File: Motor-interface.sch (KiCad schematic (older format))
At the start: 25 parts, among them K1 RELAY_2RT, P2 TE-23pins connector, Q1 Q_NPN_BCE, U1 MCP42010, U2 Teensy_3.2

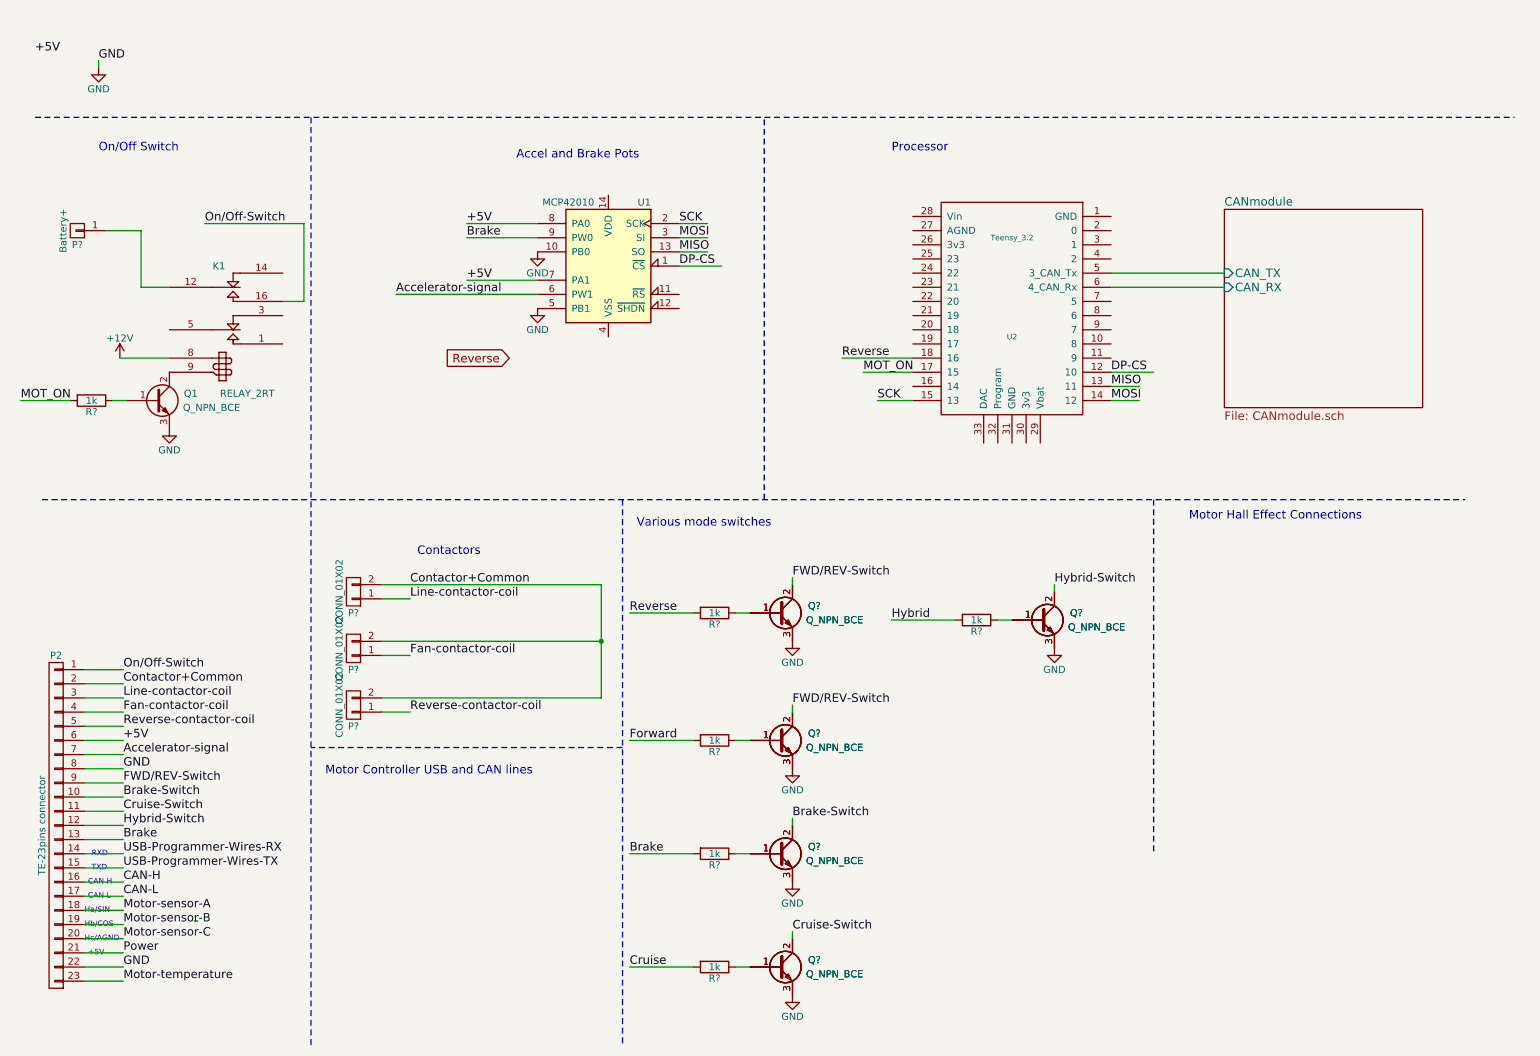
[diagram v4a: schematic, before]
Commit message: added hall effect connector and USB and CAN lines
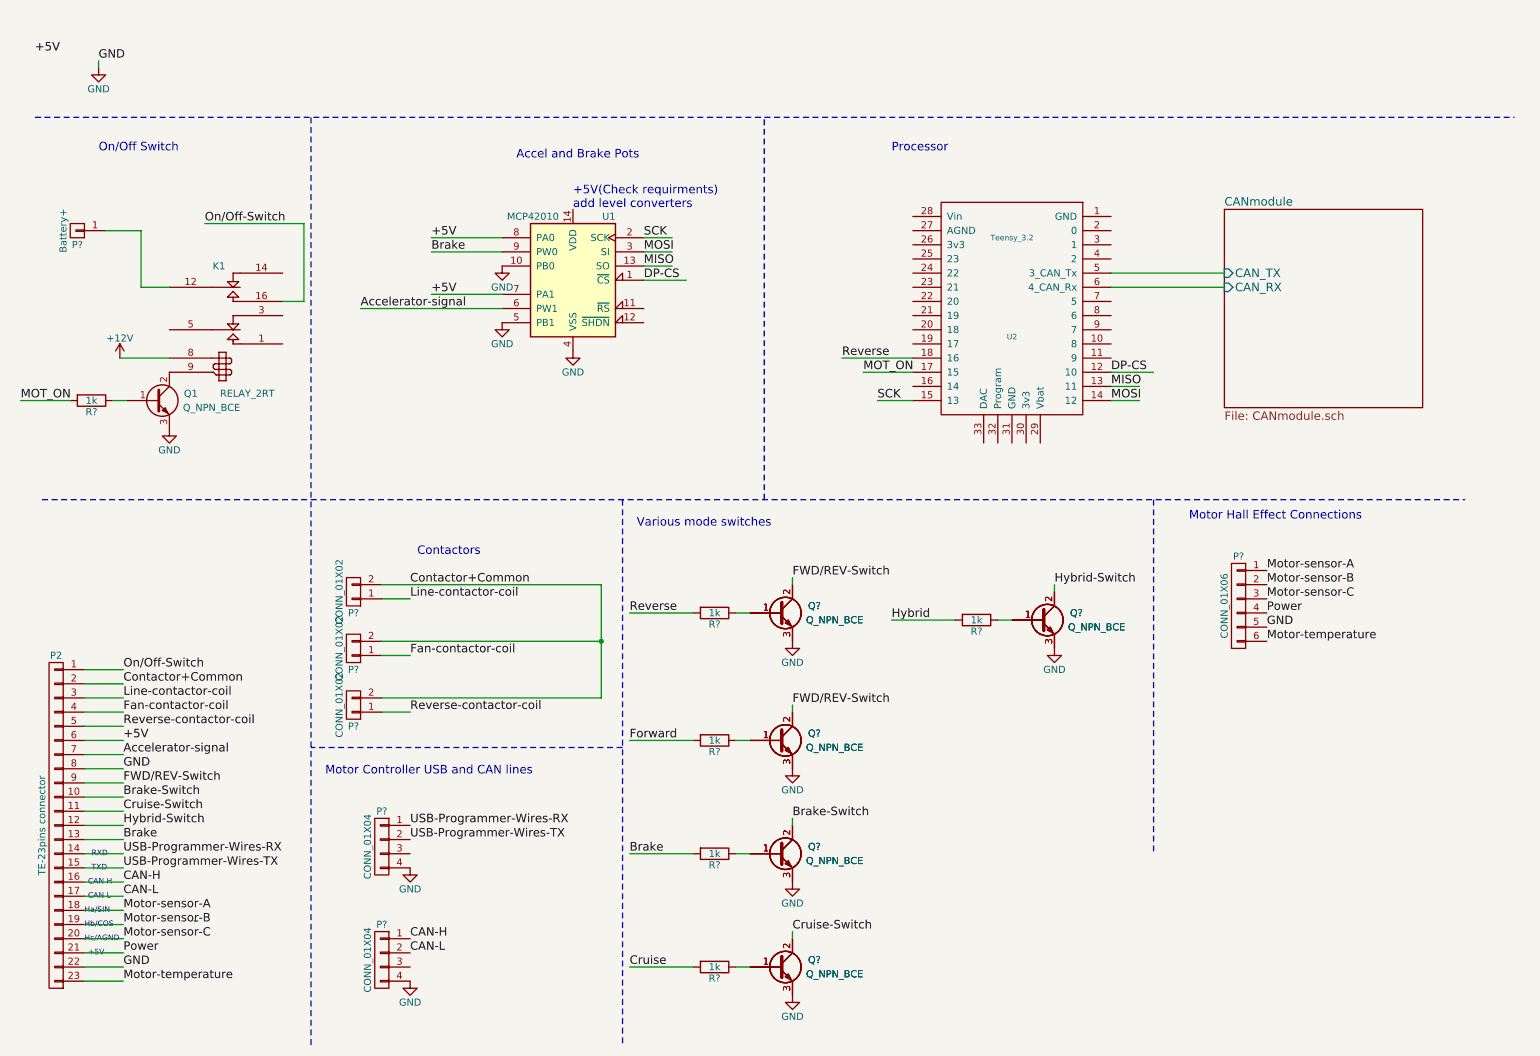
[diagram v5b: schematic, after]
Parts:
- added P?: CONN_01X06, symbol CONN_01X06
- added P? (x2): CONN_01X04, symbol CONN_01X04
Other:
- note added: "+5V(Check requirments)\nadd level converters"
- moved on the sheet: U1
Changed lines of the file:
@@
 LIBS:contrib
 LIBS:valves
-LIBS:electric_car
 LIBS:Motor-interface-cache
 EELAYER 25 0
@@
 L MCP42010 U1
 U 1 1 57FC991B
-P 4700 2300
-F 0 "U1" H 4400 2750 50  0000 L CNN
-F 1 "MCP42010" H 4800 2750 50  0000 L CNN
-F 2 "Housings_SOIC:SOIC-14_3.9x8.7mm_Pitch1.27mm" H 4700 2400 50  0001 C CNN
-F 3 "" H 4700 2400 50  0000 C CNN
-	1    4700 2300
+P 4450 2400
+F 0 "U1" H 4150 2850 50  0000 L CNN
+F 1 "MCP42010" H 4550 2850 50  0000 L CNN
+F 2 "Housings_SOIC:SOIC-14_3.9x8.7mm_Pitch1.27mm" H 4450 2500 50  0001 C CNN
+F 3 "" H 4450 2500 50  0000 C CNN
+	1    4450 2400
 	-1   0    0    -1
 $EndComp
 Wire Wire Line
-	4200 2100 3700 2100
-Text Label 3700 2100 0    60   ~ 0
+	3950 2200 3450 2200
+Text Label 3450 2200 0    60   ~ 0
 Brake
-Text GLabel 4000 2950 0    60   Input ~ 0
-Reverse
-Wire Wire Line
-	3200 2500 4200 2500
-Text Label 5200 2000 0    60   ~ 0
+Wire Wire Line
+	2950 2600 3950 2600
+Text Label 4950 2100 0    60   ~ 0
 SCK
 Wire Wire Line
@@
 	6600 3250 6850 3250
 Wire Wire Line
-	5200 2000 5400 2000
-Text Label 5200 2300 0    60   ~ 0
+	4950 2100 5150 2100
+Text Label 4950 2400 0    60   ~ 0
 DP-CS
 Text Label 8250 3050 0    60   ~ 0
@@
 	8250 3050 8550 3050
 Wire Wire Line
-	5200 2300 5500 2300
-Text Label 5200 2200 0    60   ~ 0
+	4950 2400 5250 2400
+Text Label 4950 2300 0    60   ~ 0
 MISO
-Text Label 5200 2100 0    60   ~ 0
+Text Label 4950 2200 0    60   ~ 0
 MOSI
 Wire Wire Line
-	5200 2100 5400 2100
-Wire Wire Line
-	5200 2200 5400 2200
+	4950 2200 5150 2200
+Wire Wire Line
+	4950 2300 5150 2300
 Text Label 8250 3150 0    60   ~ 0
 MISO
@@
 	6500 3050 6850 3050
 Wire Wire Line
-	3700 2400 4200 2400
+	3450 2500 3950 2500
 Wire Wire Line
 	2550 2550 2400 2550
@@
 L GND #PWR05
 U 1 1 5805B577
-P 4200 2200
-F 0 "#PWR05" H 4200 1950 50  0001 C CNN
-F 1 "GND" H 4200 2050 50  0000 C CNN
-F 2 "" H 4200 2200 50  0000 C CNN
-F 3 "" H 4200 2200 50  0000 C CNN
-	1    4200 2200
+P 3950 2300
+F 0 "#PWR05" H 3950 2050 50  0001 C CNN
+F 1 "GND" H 3950 2150 50  0000 C CNN
+F 2 "" H 3950 2300 50  0000 C CNN
+F 3 "" H 3950 2300 50  0000 C CNN
+	1    3950 2300
 	1    0    0    -1
 $EndComp
@@
 L GND #PWR06
 U 1 1 5805B5A1
-P 4200 2600
-F 0 "#PWR06" H 4200 2350 50  0001 C CNN
-F 1 "GND" H 4200 2450 50  0000 C CNN
-F 2 "" H 4200 2600 50  0000 C CNN
-F 3 "" H 4200 2600 50  0000 C CNN
-	1    4200 2600
+P 3950 2700
+F 0 "#PWR06" H 3950 2450 50  0001 C CNN
+F 1 "GND" H 3950 2550 50  0000 C CNN
+F 2 "" H 3950 2700 50  0000 C CNN
+F 3 "" H 3950 2700 50  0000 C CNN
+	1    3950 2700
 	1    0    0    -1
 $EndComp
@@
 Wire Wire Line
 	1000 7250 1275 7250
-Wire Wire Line
-	1000 7350 1275 7350
 Text Notes 1000 6875 0    39   ~ 0
 Ha/SIN
@@
 Text Label 1275 7250 0    59   ~ 0
 GND
-Text Label 1275 7350 0    59   ~ 0
-Motor-temperature
 Wire Wire Line
 	1000 5150 1275 5150
@@
 Wire Wire Line
 	1775 6925 1800 6925
-Text Label 3200 2500 0    60   ~ 0
+Text Label 2950 2600 0    60   ~ 0
 Accelerator-signal
-Text Label 3700 2400 0    60   ~ 0
+Text Label 3450 2500 0    60   ~ 0
 +5V
 Text Label 1100 850  0    59   ~ 0
@@
 Wire Wire Line
 	1100 850  1100 900
-Text Label 3700 2000 0    60   ~ 0
+Text Label 3450 2100 0    60   ~ 0
 +5V
 Wire Wire Line
-	3700 2000 4200 2000
+	3450 2100 3950 2100
 Text Notes 1100 1500 0    60   ~ 0
 On/Off Switch
@@
 Wire Notes Line
 	8550 3950 8550 6450
+$Comp
+L CONN_01X06 P?
+U 1 1 5821DB26
+P 9150 4700
+F 0 "P?" H 9150 5050 50  0000 C CNN
+F 1 "CONN_01X06" V 9250 4700 50  0000 C CNN
+F 2 "" H 9150 4700 50  0000 C CNN
+F 3 "" H 9150 4700 50  0000 C CNN
+	1    9150 4700
+	-1   0    0    -1
+$EndComp
+Text Label 9350 4450 0    59   ~ 0
+Motor-sensor-A
+Text Label 9350 4550 0    59   ~ 0
+Motor-sensor-B
+Text Label 9350 4650 0    59   ~ 0
+Motor-sensor-C
+Text Label 9350 4750 0    59   ~ 0
+Power
+Text Label 9350 4850 0    59   ~ 0
+GND
+Wire Wire Line
+	1000 7350 1275 7350
+Text Label 1275 7350 0    59   ~ 0
+Motor-temperature
+Text Label 9350 4950 0    59   ~ 0
+Motor-temperature
+$Comp
+L GND #PWR?
+U 1 1 5822F91D
+P 4450 2900
+F 0 "#PWR?" H 4450 2650 50  0001 C CNN
+F 1 "GND" H 4450 2750 50  0000 C CNN
+F 2 "" H 4450 2900 50  0000 C CNN
+F 3 "" H 4450 2900 50  0000 C CNN
+	1    4450 2900
+	1    0    0    -1
+$EndComp
+Text Notes 4450 1900 0    60   ~ 0
++5V(Check requirments)\nadd level converters
+$Comp
+L CONN_01X04 P?
+U 1 1 58232DEE
+P 3100 6400
+F 0 "P?" H 3100 6650 50  0000 C CNN
+F 1 "CONN_01X04" V 3200 6400 50  0000 C CNN
+F 2 "" H 3100 6400 50  0000 C CNN
+F 3 "" H 3100 6400 50  0000 C CNN
+	1    3100 6400
+	-1   0    0    -1
+$EndComp
+$Comp
+L CONN_01X04 P?
+U 1 1 58232EBA
+P 3100 7200
+F 0 "P?" H 3100 7450 50  0000 C CNN
+F 1 "CONN_01X04" V 3200 7200 50  0000 C CNN
+F 2 "" H 3100 7200 50  0000 C CNN
+F 3 "" H 3100 7200 50  0000 C CNN
+	1    3100 7200
+	-1   0    0    -1
+$EndComp
+Text Label 3300 6250 0    60   ~ 0
+USB-Programmer-Wires-RX
+Text Label 3300 6350 0    59   ~ 0
+USB-Programmer-Wires-TX
+Text Label 3300 7050 0    59   ~ 0
+CAN-H
+Text Label 3300 7150 0    59   ~ 0
+CAN-L
+$Comp
+L GND #PWR?
+U 1 1 5823333B
+P 3300 6550
+F 0 "#PWR?" H 3300 6300 50  0001 C CNN
+F 1 "GND" H 3300 6400 50  0000 C CNN
+F 2 "" H 3300 6550 50  0000 C CNN
+F 3 "" H 3300 6550 50  0000 C CNN
+	1    3300 6550
+	1    0    0    -1
+$EndComp
+$Comp
+L GND #PWR?
+U 1 1 5823340C
+P 3300 7350
+F 0 "#PWR?" H 3300 7100 50  0001 C CNN
+F 1 "GND" H 3300 7200 50  0000 C CNN
+F 2 "" H 3300 7350 50  0000 C CNN
+F 3 "" H 3300 7350 50  0000 C CNN
+	1    3300 7350
+	1    0    0    -1
+$EndComp
 $EndSCHEMATC

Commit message: added hall-uC resistors for speed monitoring
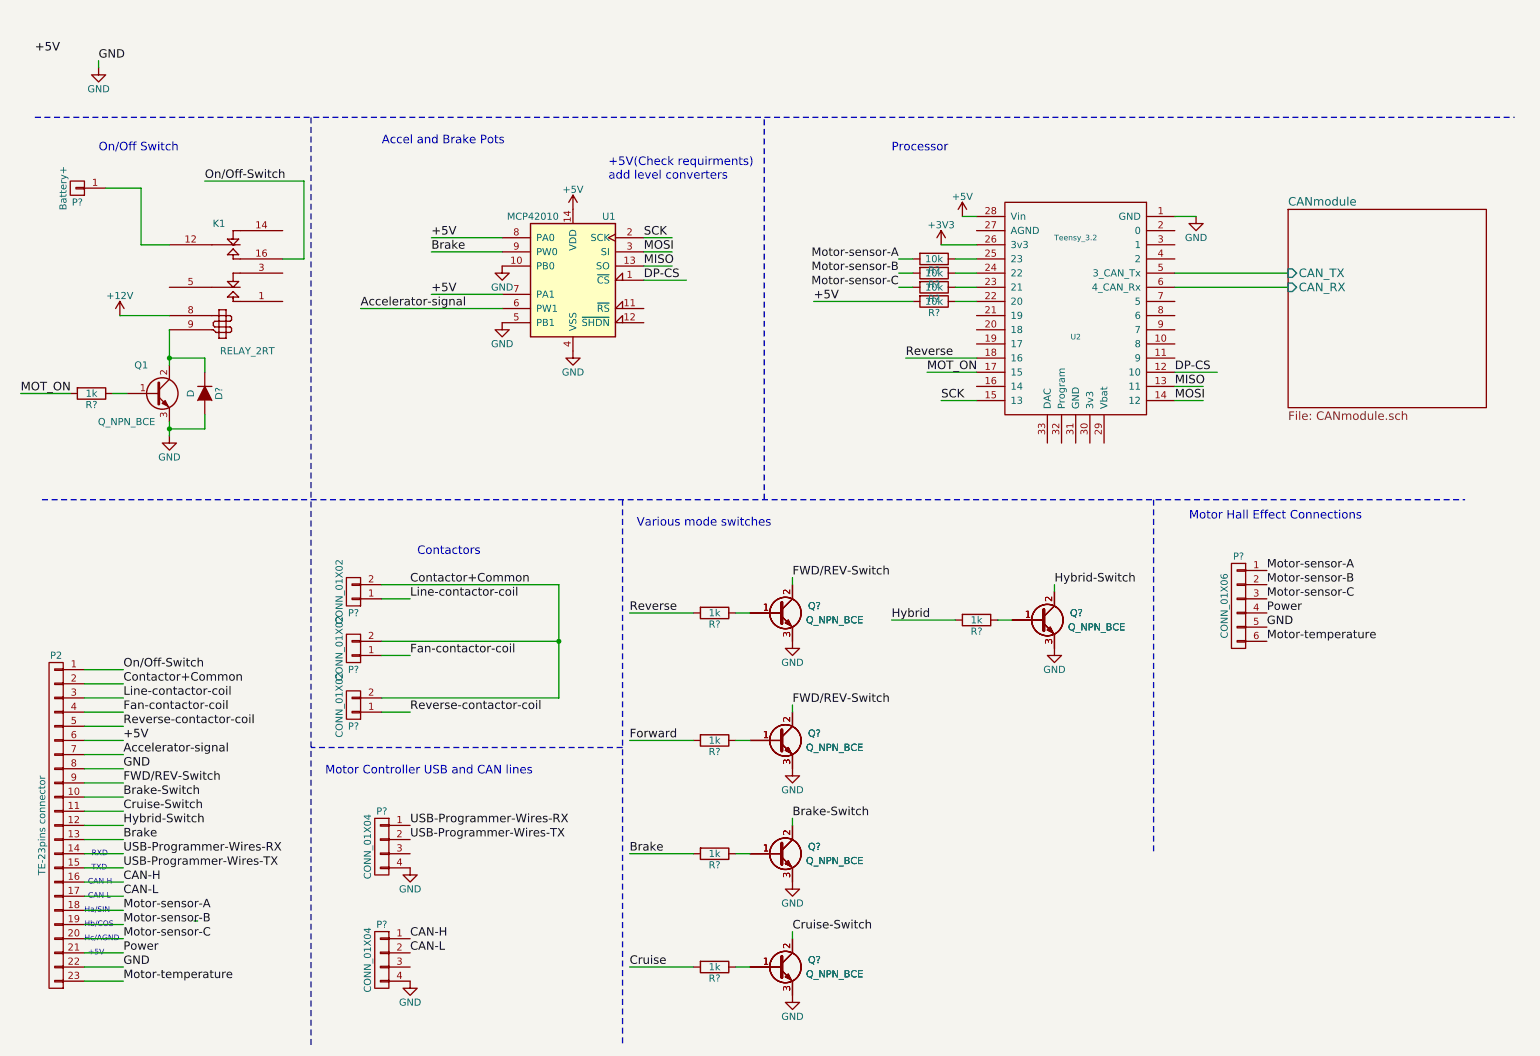
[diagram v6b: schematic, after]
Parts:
- added D?: D, symbol D
- added R? (x4): 10k, symbol R
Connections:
- net labels added: +3V3
- wire segments 72 -> 92
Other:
- moved on the sheet: K1, P?, Q1, R?, U2

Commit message: Isolated the Motor Controller, added PSU
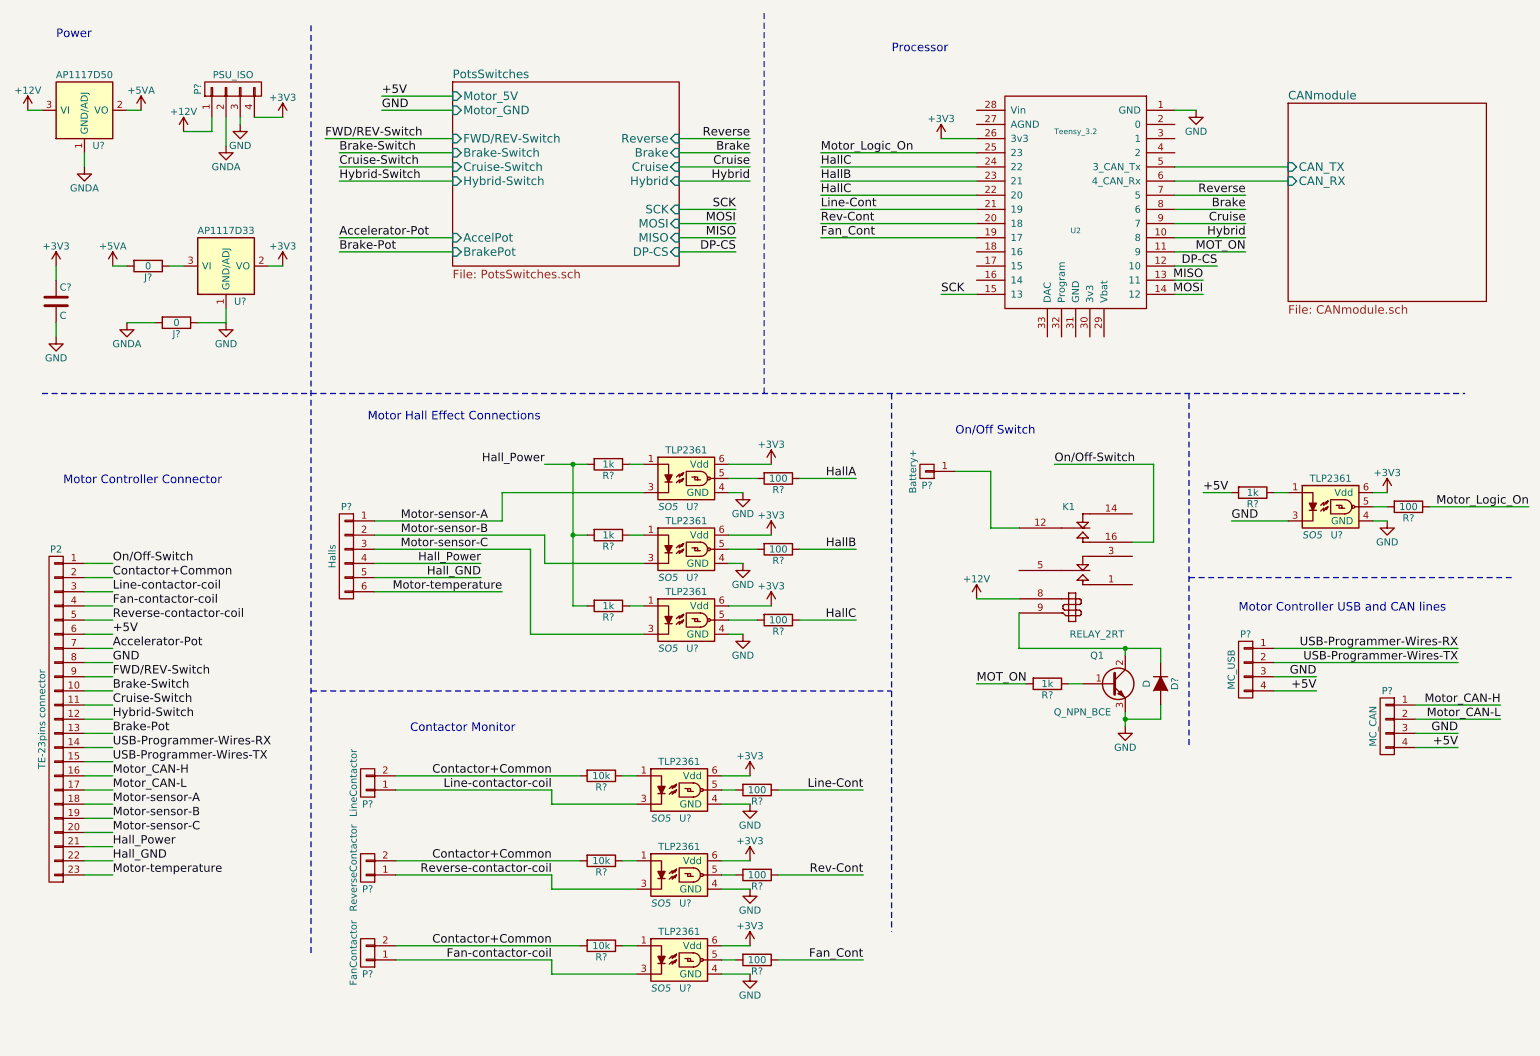
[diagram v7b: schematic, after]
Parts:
- removed Q? (x10): Q_NPN_BCE, TO_SOT_Packages_SMD:SOT-23, symbol Q_NPN_BCE
- removed R? (x5): 1k, symbol R
- removed R? (x4): 10k, symbol R
- removed U1: MCP42010, Housings_SOIC:SOIC-14_3.9x8.7mm_Pitch1.27mm, symbol MCP42010
- added C?: C, symbol C
- added J? (x2): 0, symbol R
- added P?: PSU_ISO, symbol CONN_01X04
- added R? (x3): 10k, symbol R
- added R? (x7): 100, symbol R
- added R? (x4): 1k, symbol R
- added U? (x7): TLP2361, SO5, symbol TLP2361
- added U?: AP1117D33, symbol AP1117D33
- added U?: AP1117D50, symbol AP1117D50
- P?: value CONN_01X02 -> LineContactor
- P?: value CONN_01X02 -> FanContactor
- P?: value CONN_01X02 -> ReverseContactor
- P?: value CONN_01X06 -> Halls
- P?: value CONN_01X04 -> MC_USB
- P?: value CONN_01X04 -> MC_CAN
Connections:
- net labels added: +5VA, Accelerator-Pot, Brake-Pot, Fan_Cont, GNDA, HallA, HallB, HallC, Hall_GND, Hall_Power, Line-Cont, Motor_CAN-H, Motor_CAN-L, Motor_Logic_On, Rev-Cont
- net labels removed: Accelerator-signal, CAN-H, CAN-L, Forward, Power
- wire segments 92 -> 164
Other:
- note added: "Contactor Monitor"
- note added: "Motor Controller Connector"
- note added: "Power"
- note removed: "+5V"
- note removed: "+5V(Check requirments)\nadd level converters"
- note removed: "Accel and Brake Pots"
- note removed: "CAN H"
- note removed: "CAN L"
- note removed: "Contactors"
- note removed: "Ha/SIN"
- note removed: "Hb/COS"
- note removed: "Hc/AGND"
- note removed: "RXD"
- note removed: "TXD"
- note removed: "Various mode switches"
- moved on the sheet: D?, K1, P2, P?, Q1, R?, U2
